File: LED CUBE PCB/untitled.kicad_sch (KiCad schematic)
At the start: 46 parts, among them J1 Conn_01x06, J3 Conn_01x09, SW1 BZCN_TSA007A1518B03, U1 TPS7A2633DRVR, U2 CH340C, Y3 8MHz, Y4 32.786KHz

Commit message: Beginning PCB layout
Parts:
- removed MC3: STM32F103, Borna KiCAD Library:TQFP48, symbol STM32F103c:STM32F103
- added MCU1: STM32F103, Borna KiCAD Library:TQFP48, symbol STM32F103c:STM32F103
- R4, R5, R7: footprint Resistor_SMD:R_0201_0603Metric -> Borna KiCAD Library:R0603
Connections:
- net 3V3: now also MCU1.36 (VCC), MCU1.48 (VCC3V3)
- net BOOT0: now also MCU1.44 (BOOT)
- net BOOT1: now also MCU1.20 (PB2)
- net DN: now also MCU1.32 (PA11)
- net DP: now also MCU1.33 (PA12)
- net GND: now also MCU1.23 (VSS), MCU1.35 (GND), MCU1.47 (GND), MCU1.8 (VSSA_GND)
- net OE: now also MCU1.25 (PB12)
- net OSCIN: now also MCU1.5 (OSCIN)
- net OSCOUT: now also MCU1.6 (OSOUT)
- net PA0: now also MCU1.10 (PA0)
- net PA1: now also MCU1.11 (PA1)
- net PA10: now also MCU1.31 (PA10)
- net PA15: now also MCU1.38 (PA15)
- net PA2: now also MCU1.12 (PA2)
- net PA3: now also MCU1.13 (PA3)
- net PA4: now also MCU1.14 (PA4)
- net PA5: now also MCU1.15 (PA5)
- net PA6: now also MCU1.16 (PA6)
- net PA7: now also MCU1.17 (PA7)
- net PA8: now also MCU1.29 (PA8)
- net PA9: now also MCU1.30 (PA9)
- net PB0: now also MCU1.18 (PB0)
- net PB1: now also MCU1.19 (PB1)
- net PB10: now also MCU1.21 (PB10)
- net PB11: now also MCU1.22 (PB11)
- net PB13: now also MCU1.26 (PB13)
- net PB14: now also MCU1.27 (PB14)
- net PB15: now also MCU1.28 (PB15)
- net PB3: now also MCU1.39 (PB3)
- net PB4: now also MCU1.40 (PB4)
- net PB5: now also MCU1.41 (PB5)
- net PB6: now also MCU1.42 (PB6)
- net PB7: now also MCU1.43 (PB7)
- net PB8: now also MCU1.45 (PB8)
- net PB9: now also MCU1.46 (PB9)
- net PC13: now also MCU1.2 (PC13)
- net PC14: now also MCU1.3 (PC14)
- net PC15: now also MCU1.4 (PC15)
- net RESET: now also MCU1.7 (NRST)
- net SWIO: now also MCU1.34 (SWIO)
- net SWLCK: now also MCU1.37 (SWCLK)
- net VBAT: now also MCU1.1 (VCC)
- net VCC3V3: now also MCU1.24 (VDD), MCU1.9 (VDDA)
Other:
- note added: "STM32F103C6"
- note removed: "STM32F103C6T1"
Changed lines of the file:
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@@
 		)
 	)
-	(text "STM32F103C6T1"
+	(text "STM32F103C6"
 		(exclude_from_sim no)
 		(at 226.314 17.018 0)
@@
 			)
 		)
-		(property "Footprint" "Resistor_SMD:R_0201_0603Metric"
+		(property "Footprint" "Borna KiCAD Library:R0603"
 			(at 193.04 123.698 90)
 			(effects
@@
 			)
 		)
-		(property "Footprint" "Resistor_SMD:R_0201_0603Metric"
+		(property "Footprint" "Borna KiCAD Library:R0603"
 			(at 205.74 121.158 90)
 			(effects
@@
 			)
 		)
-		(property "Description" ""
+		(property "Description" "Resistor"
 			(at 205.74 119.38 0)
 			(effects
@@
 					(size 1.27 1.27)
 				)
+				(hide yes)
 			)
 		)
@@
 			)
 		)
-		(property "Footprint" "Resistor_SMD:R_0201_0603Metric"
+		(property "Footprint" "Borna KiCAD Library:R0603"
 			(at 254 126.238 90)
 			(effects
@@
 	)
 	(symbol
+		(lib_id "STM32F103c:STM32F103")
+		(at 229.87 55.88 0)
+		(unit 1)
+		(exclude_from_sim no)
+		(in_bom yes)
+		(on_board yes)
+		(dnp no)
+		(property "Reference" "MCU1"
+			(at 230.124 20.32 0)
+			(effects
+				(font
+					(size 1.27 1.27)
+				)
+			)
+		)
+		(property "Value" "STM32F103"
+			(at 230.378 22.606 0)
+			(effects
+				(font
+					(size 1.27 1.27)
+				)
+			)
+		)
+		(property "Footprint" "Borna KiCAD Library:TQFP48"
+			(at 229.87 55.88 0)
+			(effects
+				(font
+					(size 1.27 1.27)
+				)
+				(hide yes)
+			)
+		)
+		(property "Datasheet" ""
+			(at 229.87 55.88 0)
+			(effects
+				(font
+					(size 1.27 1.27)
+				)
+				(hide yes)
+			)
+		)
+		(property "Description" ""
+			(at 229.87 55.88 0)
+			(effects
+				(font
+					(size 1.27 1.27)
+				)
+				(hide yes)
+			)
+		)
+		(pin "9"
+		)
+		(pin "35"
+		)
+		(pin "25"
+		)
+		(pin "5"
+		)
+		(pin "23"
+		)
+		(pin "42"
+		)
+		(pin "15"
+		)
+		(pin "31"
+		)
+		(pin "44"
+		)
+		(pin "29"
+		)
+		(pin "20"
+		)
+		(pin "3"
+		)
+		(pin "30"
+		)
+		(pin "7"
+		)
+		(pin "8"
+		)
+		(pin "19"
+		)
+		(pin "26"
+		)
+		(pin "13"
+		)
+		(pin "34"
+		)
+		(pin "14"
+		)
+		(pin "28"
+		)
+		(pin "1"
+		)
+		(pin "2"
+		)
+		(pin "4"
+		)
+		(pin "18"
+		)
+		(pin "12"
+		)
+		(pin "16"
+		)
+		(pin "10"
+		)
+		(pin "17"
+		)
+		(pin "24"
+		)
+		(pin "27"
+		)
+		(pin "33"
+		)
+		(pin "32"
+		)
+		(pin "37"
+		)
+		(pin "38"
+		)
+		(pin "39"
+		)
+		(pin "41"
+		)
+		(pin "45"
+		)
+		(pin "40"
+		)
+		(pin "11"
+		)
+		(pin "6"
+		)
+		(pin "21"
+		)
+		(pin "22"
+		)
+		(pin "36"
+		)
+		(pin "46"
+		)
+		(pin "47"
+		)
+		(pin "48"
+		)
+		(pin "43"
+		)
+		(instances
+			(project ""
+				(path "/64eb2d32-222b-4351-90b6-2cc90b760e62/ccca4637-6427-4f45-abce-b48cba1912e2"
+					(reference "MCU1")
+					(unit 1)
+				)
+			)
+		)
+	)
+	(symbol
 		(lib_id "Device:C")
 		(at 247.65 161.29 90)
@@
 					(unit 1)
 				)
-			)
-		)
-	)
-	(symbol
-		(lib_id "STM32F103c:STM32F103")
-		(at 229.87 55.88 0)
-		(unit 1)
-		(exclude_from_sim no)
-		(in_bom yes)
-		(on_board yes)
-		(dnp no)
-		(property "Reference" "MC3"
-			(at 229.616 21.082 0)
-			(effects
-				(font
-					(size 1.27 1.27)
-				)
-			)
-		)
-		(property "Value" "STM32F103"
-			(at 229.616 23.114 0)
-			(effects
-				(font
-					(size 1.27 1.27)
-				)
-			)
-		)
-		(property "Footprint" "Borna KiCAD Library:TQFP48"
-			(at 229.87 55.88 0)
-			(effects
-				(font
-					(size 1.27 1.27)
-				)
-				(hide yes)
-			)
-		)
-		(property "Datasheet" ""
-			(at 229.87 55.88 0)
-			(effects
-				(font
-					(size 1.27 1.27)
-				)
-				(hide yes)
-			)
-		)
-		(property "Description" ""
-			(at 229.87 55.88 0)
-			(effects
-				(font
-					(size 1.27 1.27)
-				)
-				(hide yes)
-			)
-		)
-		(pin "21"
-		)
-		(pin "27"
-		)
-		(pin "31"
-		)
-		(pin "22"
-		)
-		(pin "32"
-		)
-		(pin "44"
-		)
-		(pin "29"
-		)
-		(pin "26"
-		)
-		(pin "48"
-		)
-		(pin "15"
-		)
-		(pin "9"
-		)
-		(pin "43"
-		)
-		(pin "11"
-		)
-		(pin "5"
-		)
-		(pin "13"
-		)
-		(pin "19"
-		)
-		(pin "30"
-		)
-		(pin "24"
-		)
-		(pin "25"
-		)
-		(pin "42"
-		)
-		(pin "35"
-		)
-		(pin "14"
-		)
-		(pin "20"
-		)
-		(pin "37"
-		)
-		(pin "12"
-		)
-		(pin "36"
-		)
-		(pin "40"
-		)
-		(pin "39"
-		)
-		(pin "1"
-		)
-		(pin "3"
-		)
-		(pin "8"
-		)
-		(pin "16"
-		)
-		(pin "4"
-		)
-		(pin "2"
-		)
-		(pin "10"
-		)
-		(pin "7"
-		)
-		(pin "6"
-		)
-		(pin "17"
-		)
-		(pin "18"
-		)
-		(pin "23"
-		)
-		(pin "28"
-		)
-		(pin "34"
-		)
-		(pin "38"
-		)
-		(pin "41"
-		)
-		(pin "33"
-		)
-		(pin "45"
-		)
-		(pin "46"
-		)
-		(pin "47"
-		)
-		(instances
-			(project ""
-				(path "/64eb2d32-222b-4351-90b6-2cc90b760e62/ccca4637-6427-4f45-abce-b48cba1912e2"
-					(reference "MC3")
-					(unit 1)
-				)

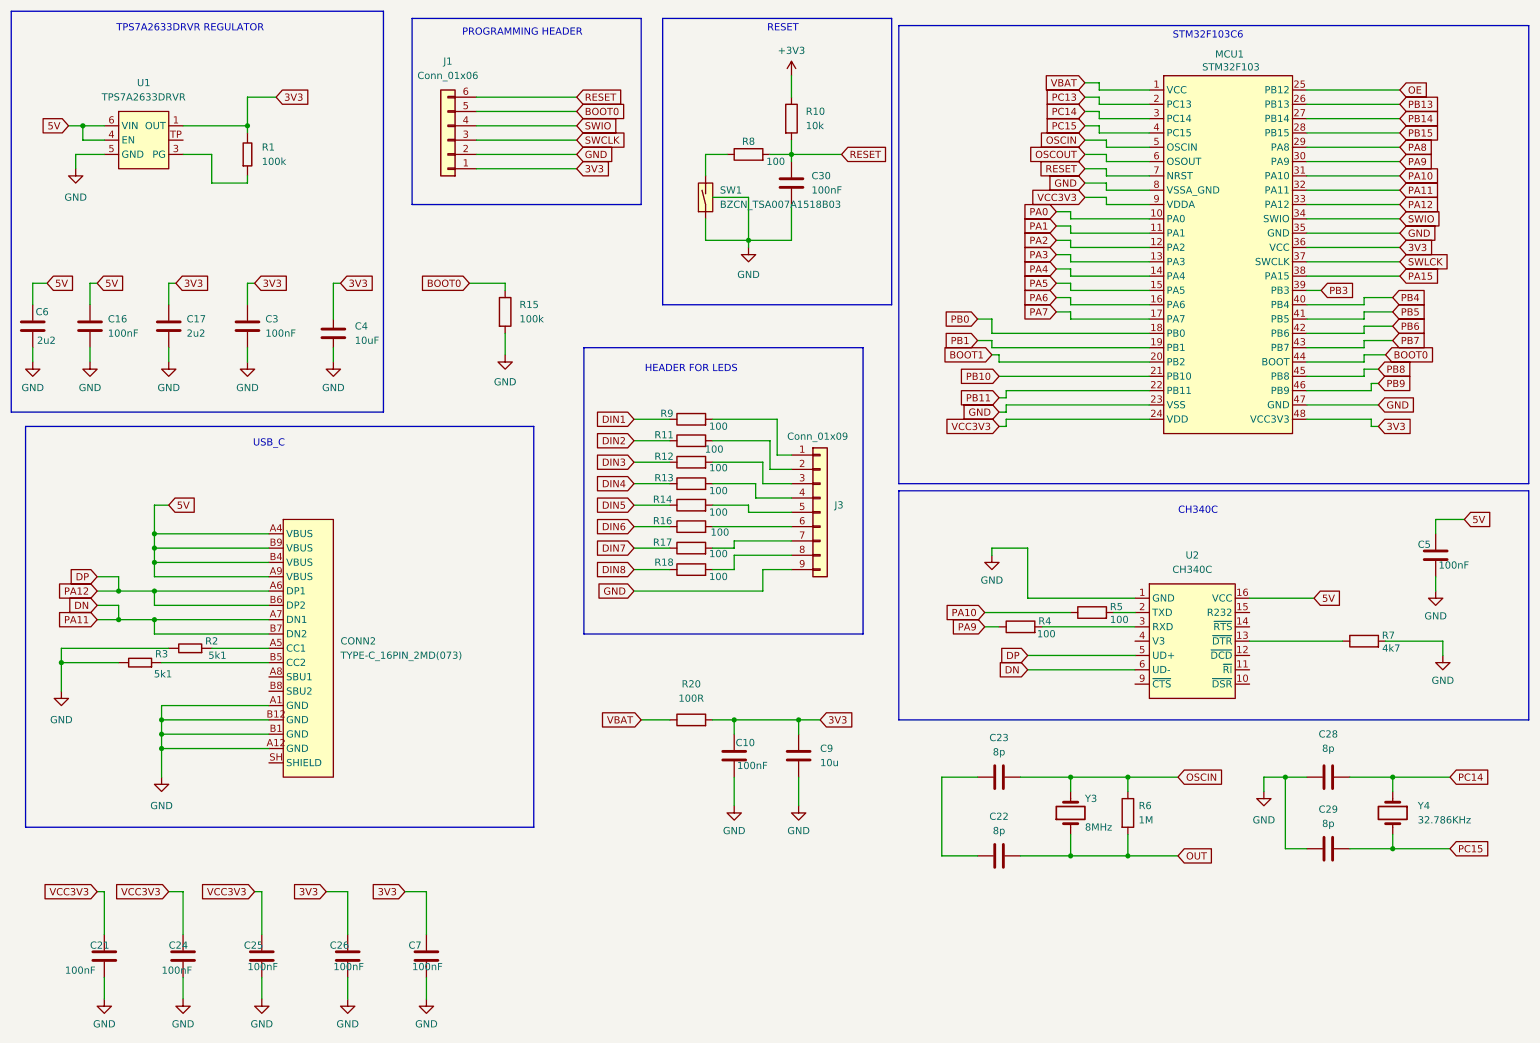
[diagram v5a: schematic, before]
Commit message: Change footprint for capacitors and routing PCB
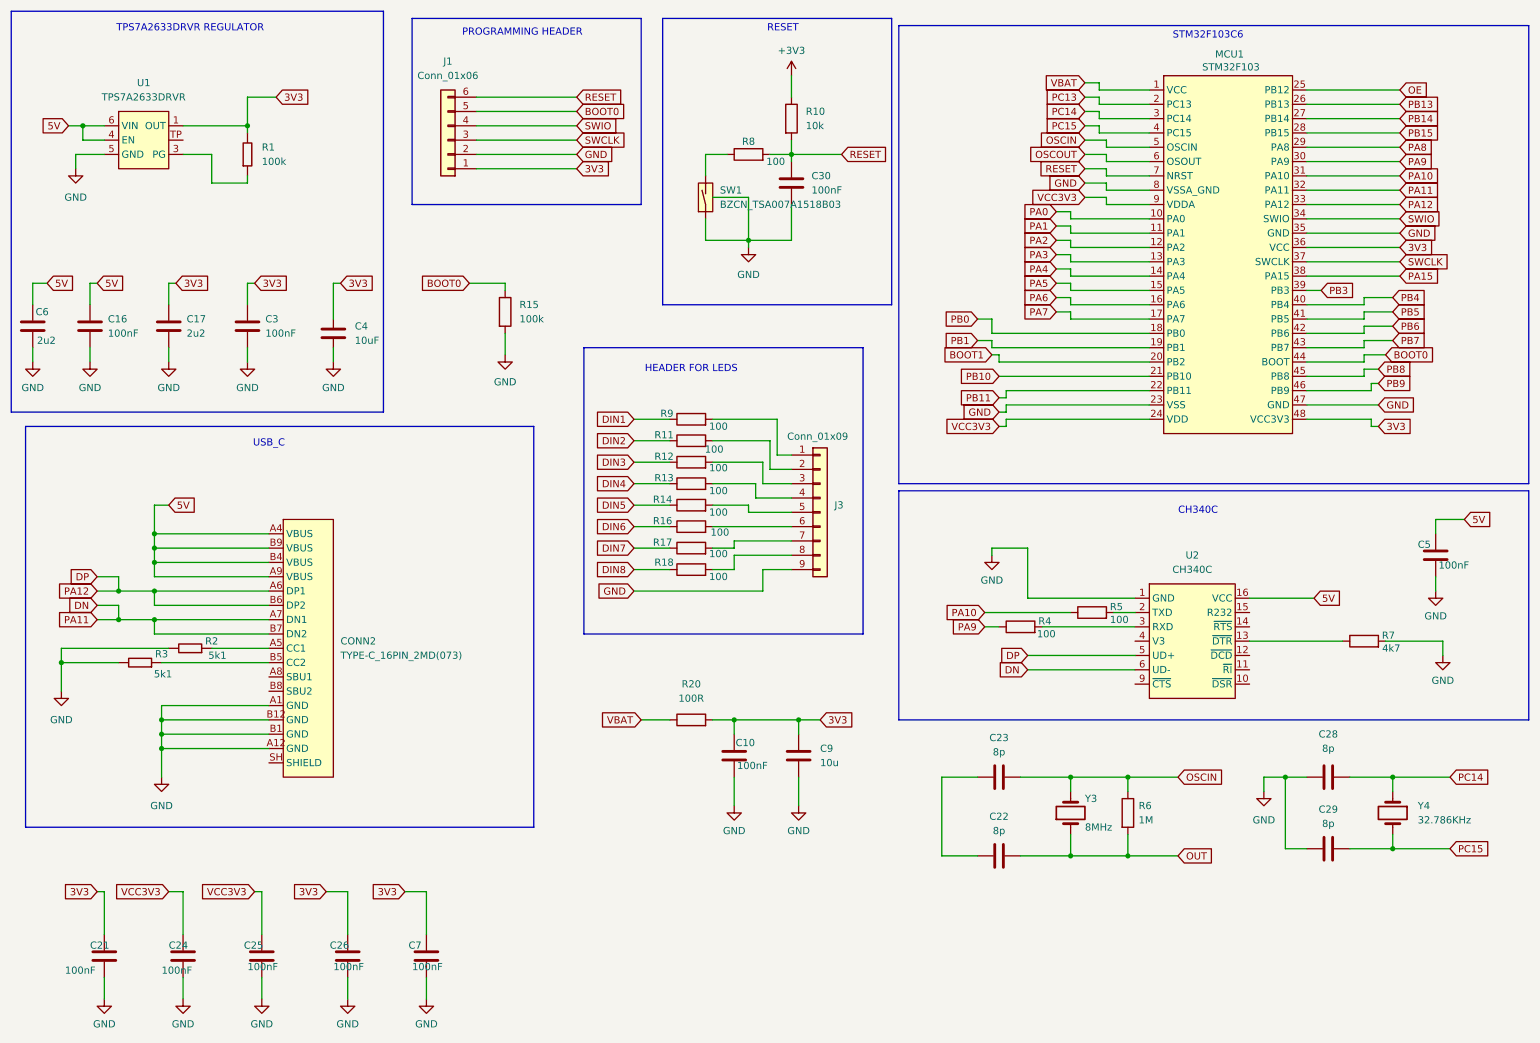
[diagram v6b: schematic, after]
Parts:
- C21: footprint Capacitor_SMD:C_0201_0603Metric -> Borna KiCAD Library:C0603
- C24, C25, C26, C7: footprint Capacitor_SMD:C_0201_0603Metric_Pad0.64x0.40mm_HandSolder -> Borna KiCAD Library:C0603
- C30: footprint Capacitor_SMD:C_0201_0603Metric -> Borna KiCAD Library:R0603
- R10: footprint Resistor_SMD:R_0201_0603Metric -> Borna KiCAD Library:R0603
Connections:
- net SWLCK is gone; now on net SWCLK: MCU1.37 (SWCLK)
- net 3V3: now also C21.1
- net VCC3V3: no longer C21.1
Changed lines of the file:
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@@
 		)
 	)
-	(global_label "SWLCK"
+	(global_label "SWCLK"
 		(shape input)
 		(at 260.35 57.15 0)
@@
 		)
 	)
-	(global_label "VCC3V3"
+	(global_label "3V3"
 		(shape input)
 		(at 29.21 168.91 180)
@@
 		)
 		(property "Intersheetrefs" "${INTERSHEET_REFS}"
-			(at 19.0886 168.91 0)
+			(at 22.7172 168.91 0)
 			(effects
 				(font
@@
 			)
 		)
-		(property "Footprint" "Capacitor_SMD:C_0201_0603Metric"
+		(property "Footprint" "Borna KiCAD Library:R0603"
 			(at 153.3652 46.99 0)
 			(effects
@@
 			)
 		)
-		(property "Footprint" "Resistor_SMD:R_0201_0603Metric"
+		(property "Footprint" "Borna KiCAD Library:R0603"
 			(at 150.622 31.75 90)
 			(effects
@@
 			)
 		)
-		(property "Footprint" "Capacitor_SMD:C_0201_0603Metric_Pad0.64x0.40mm_HandSolder"
+		(property "Footprint" "Borna KiCAD Library:C0603"
 			(at 88.5952 184.15 0)
 			(effects
@@
 			)
 		)
-		(property "Footprint" "Capacitor_SMD:C_0201_0603Metric_Pad0.64x0.40mm_HandSolder"
+		(property "Footprint" "Borna KiCAD Library:C0603"
 			(at 45.4152 184.15 0)
 			(effects
@@
 			)
 		)
-		(property "Footprint" "Capacitor_SMD:C_0201_0603Metric_Pad0.64x0.40mm_HandSolder"
+		(property "Footprint" "Borna KiCAD Library:C0603"
 			(at 59.3852 184.15 0)
 			(effects
@@
 			)
 		)
-		(property "Footprint" "Capacitor_SMD:C_0201_0603Metric_Pad0.64x0.40mm_HandSolder"
+		(property "Footprint" "Borna KiCAD Library:C0603"
 			(at 74.6252 184.15 0)
 			(effects
@@
 			)
 		)
-		(property "Footprint" "Capacitor_SMD:C_0201_0603Metric"
+		(property "Footprint" "Borna KiCAD Library:C0603"
 			(at 31.4452 184.15 0)
 			(effects

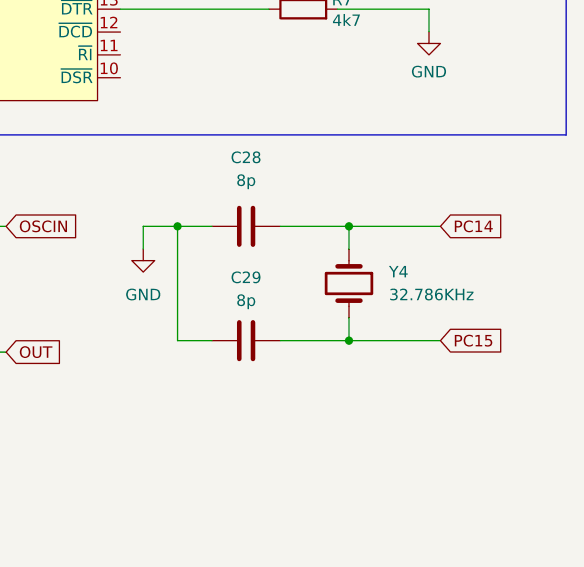
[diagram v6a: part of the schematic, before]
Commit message: Change footprint for crystal
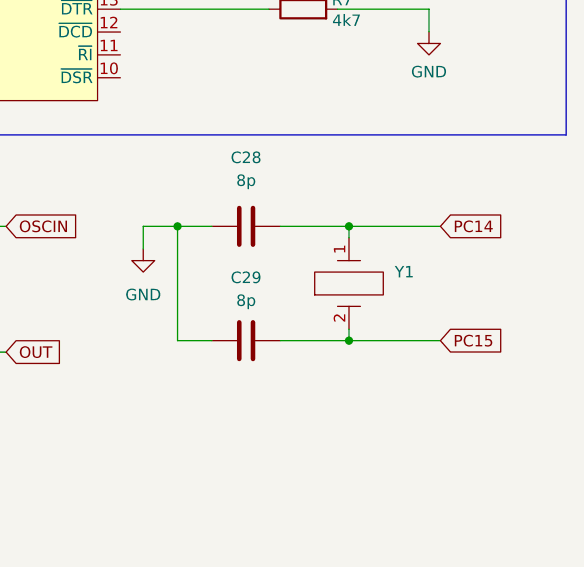
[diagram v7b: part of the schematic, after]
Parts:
- removed Y4: 32.786KHz, Crystal:Crystal_HC49-4H_Vertical, symbol Device:Crystal
- added Y1: ~, Marina_Library:SMD3215-2P, symbol Marina_Library:NX3215SA-32.768K-STD-MUA-8
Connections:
- net PC14: now also Y1.1
- net PC15: now also Y1.2
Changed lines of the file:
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@@
 	)
 	(junction
-		(at 259.08 161.29)
-		(diameter 0)
-		(color 0 0 0 0)
-	)
-	(junction
 		(at 33.02 115.57)
 		(diameter 0)
@@
 	)
 	(junction
-		(at 259.08 148.59)
+		(at 212.09 162.56)
 		(diameter 0)
 		(color 0 0 0 0)
 	)
 	(junction
-		(at 212.09 162.56)
+		(at 259.08 161.29)
 		(diameter 0)
 		(color 0 0 0 0)
@@
 	)
 	(junction
+		(at 259.08 148.59)
+		(diameter 0)
+		(color 0 0 0 0)
+	)
+	(junction
 		(at 212.09 148.59)
 		(diameter 0)
@@
 	(wire
 		(pts
-			(xy 259.08 161.29) (xy 269.24 161.29)
-		)
-		(stroke
-			(width 0)
-			(type default)
-		)
-	)
-	(wire
-		(pts
 			(xy 39.37 120.65) (xy 59.69 120.65)
 		)
@@
 	(wire
 		(pts
+			(xy 259.08 161.29) (xy 269.24 161.29)
+		)
+		(stroke
+			(width 0)
+			(type default)
+		)
+	)
+	(wire
+		(pts
 			(xy 142.24 138.43) (xy 142.24 140.97)
 		)
@@
 	(wire
 		(pts
-			(xy 259.08 151.13) (xy 259.08 148.59)
-		)
-		(stroke
-			(width 0)
-			(type default)
-		)
-	)
-	(wire
-		(pts
 			(xy 142.24 106.68) (xy 142.24 107.95)
 		)
@@
 	(wire
 		(pts
-			(xy 259.08 158.75) (xy 259.08 161.29)
-		)
-		(stroke
-			(width 0)
-			(type default)
-		)
-	)
-	(wire
-		(pts
 			(xy 29.21 118.11) (xy 33.02 118.11)
 		)
@@
 	(wire
 		(pts
+			(xy 259.08 160.02) (xy 259.08 161.29)
+		)
+		(stroke
+			(width 0)
+			(type default)
+		)
+	)
+	(wire
+		(pts
 			(xy 215.9 39.37) (xy 208.28 39.37)
 		)
@@
 	(wire
 		(pts
+			(xy 259.08 148.59) (xy 259.08 149.86)
+		)
+		(stroke
+			(width 0)
+			(type default)
+		)
+	)
+	(wire
+		(pts
 			(xy 201.93 52.07) (xy 201.93 50.8)
 		)
@@
 	(wire
 		(pts
+			(xy 259.08 148.59) (xy 269.24 148.59)
+		)
+		(stroke
+			(width 0)
+			(type default)
+		)
+	)
+	(wire
+		(pts
 			(xy 215.9 52.07) (xy 201.93 52.07)
 		)
@@
 	(wire
 		(pts
-			(xy 259.08 148.59) (xy 269.24 148.59)
-		)
-		(stroke
-			(width 0)
-			(type default)
-		)
-	)
-	(wire
-		(pts
 			(xy 55.88 60.96) (xy 57.15 60.96)
 		)
@@
 	)
 	(symbol
+		(lib_id "Marina_Library:NX3215SA-32.768K-STD-MUA-8")
+		(at 259.08 154.94 90)
+		(unit 1)
+		(exclude_from_sim no)
+		(in_bom yes)
+		(on_board yes)
+		(dnp no)
+		(fields_autoplaced yes)
+		(property "Reference" "Y1"
+			(at 264.16 153.6699 90)
+			(effects
+				(font
+					(size 1.27 1.27)
+				)
+				(justify right)
+			)
+		)
+		(property "Value" "~"
+			(at 264.16 156.2099 90)
+			(effects
+				(font
+					(size 1.27 1.27)
+				)
+				(justify right)
+			)
+		)
+		(property "Footprint" "Marina_Library:SMD3215-2P"
+			(at 263.906 155.194 0)
+			(effects
+				(font
+					(size 1.27 1.27)
+				)
+				(hide yes)
+			)
+		)
+		(property "Datasheet" ""
+			(at 259.08 154.94 0)
+			(effects
+				(font
+					(size 1.27 1.27)
+				)
+				(hide yes)
+			)
+		)
+		(property "Description" ""
+			(at 259.08 154.94 0)
+			(effects
+				(font
+					(size 1.27 1.27)
+				)
+				(hide yes)
+			)
+		)
+		(pin "2"
+		)
+		(pin "1"
+		)
+		(instances
+			(project ""
+				(path "/64eb2d32-222b-4351-90b6-2cc90b760e62/ccca4637-6427-4f45-abce-b48cba1912e2"
+					(reference "Y1")
+					(unit 1)
+				)
+			)
+		)
+	)
+	(symbol
 		(lib_id "Borna KiCAD Library:TYPE-C_16PIN_2MD(073)")
 		(at 66.04 125.73 0)
@@
 					(unit 1)
 				)
-			)
-		)
-	)
-	(symbol
-		(lib_id "Device:Crystal")
-		(at 259.08 154.94 270)
-		(unit 1)
-		(exclude_from_sim no)
-		(in_bom yes)
-		(on_board yes)
-		(dnp no)
-		(fields_autoplaced yes)
-		(property "Reference" "Y4"
-			(at 263.525 153.67 90)
-			(effects
-				(font
-					(size 1.27 1.27)
-				)
-				(justify left)
-			)
-		)
-		(property "Value" "32.786KHz"
-			(at 263.525 156.21 90)
-			(effects
-				(font
-					(size 1.27 1.27)
-				)
-				(justify left)
-			)
-		)
-		(property "Footprint" "Crystal:Crystal_HC49-4H_Vertical"
-			(at 259.08 154.94 0)
-			(effects
-				(font
-					(size 1.27 1.27)
-				)
-				(hide yes)
-			)
-		)
-		(property "Datasheet" "~"
-			(at 259.08 154.94 0)
-			(effects
-				(font
-					(size 1.27 1.27)
-				)
-				(hide yes)
-			)
-		)
-		(property "Description" ""
-			(at 259.08 154.94 0)
-			(effects
-				(font
-					(size 1.27 1.27)
-				)
-			)
-		)
-		(pin "1"
-		)
-		(pin "2"
-		)
-		(instances
-			(project "LED CUBE PCB"
-				(path "/64eb2d32-222b-4351-90b6-2cc90b760e62/ccca4637-6427-4f45-abce-b48cba1912e2"
-					(reference "Y4")
-					(unit 1)
-				)

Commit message: Updated PCB
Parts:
- C22, C23, C28, C29: footprint Capacitor_SMD:C_0201_0603Metric_Pad0.64x0.40mm_HandSolder -> Borna KiCAD Library:C0603
- R6: footprint Capacitor_SMD:C_0201_0603Metric_Pad0.64x0.40mm_HandSolder -> Borna KiCAD Library:R1206
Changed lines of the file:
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@@
 			)
 		)
-		(property "Footprint" "Capacitor_SMD:C_0201_0603Metric_Pad0.64x0.40mm_HandSolder"
+		(property "Footprint" "Borna KiCAD Library:C0603"
 			(at 251.46 147.6248 0)
 			(effects
@@
 			)
 		)
-		(property "Footprint" "Capacitor_SMD:C_0201_0603Metric_Pad0.64x0.40mm_HandSolder"
+		(property "Footprint" "Borna KiCAD Library:R1206"
 			(at 210.312 154.94 90)
 			(effects
@@
 			)
 		)
-		(property "Footprint" "Capacitor_SMD:C_0201_0603Metric_Pad0.64x0.40mm_HandSolder"
+		(property "Footprint" "Borna KiCAD Library:C0603"
 			(at 185.42 149.5552 0)
 			(effects
@@
 			)
 		)
-		(property "Footprint" "Capacitor_SMD:C_0201_0603Metric_Pad0.64x0.40mm_HandSolder"
+		(property "Footprint" "Borna KiCAD Library:C0603"
 			(at 251.46 160.3248 0)
 			(effects
@@
 			)
 		)
-		(property "Footprint" "Capacitor_SMD:C_0201_0603Metric_Pad0.64x0.40mm_HandSolder"
+		(property "Footprint" "Borna KiCAD Library:C0603"
 			(at 185.42 163.5252 0)
 			(effects
